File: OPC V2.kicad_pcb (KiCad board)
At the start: 4 copper layers, 65 x 43 mm, 51 parts, among them J1 691382010004, J2 691382010004, J3 691382010004, J4 Conn_01x04_Pin, J6 Conn_01x05, J7 MEC1-110-02-F-D-A, U10 BMP581, U6 ADS1120-PW, U7 MCP23017x-x-ML, U9 DS3231MZ

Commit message: maj puissance
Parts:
- added C13: 0.1µ, Capacitor_SMD:C_0603_1608Metric_Pad1.08x0.95mm_HandSolder, F.Cu at (114.6, 63.6)
- added C14: 0.1µ, Capacitor_SMD:C_0603_1608Metric_Pad1.08x0.95mm_HandSolder, F.Cu at (114.6, 58.5)
- added C15: 4µ7 50V, Capacitor_SMD:C_1206_3216Metric, F.Cu at (150.6, 54.4)
- added C16: 4µ7 50V, Capacitor_SMD:C_1206_3216Metric, F.Cu at (144.2, 54.4)
- added C17: 10µ 10V, Capacitor_SMD:C_0603_1608Metric_Pad1.08x0.95mm_HandSolder, F.Cu at (151.0, 60.1)
- added C18: 1n 2kV, Capacitor_SMD:C_1206_3216Metric, B.Cu at (155.0, 57.2)
- added C19: 0.1µ, Capacitor_SMD:C_0603_1608Metric_Pad1.08x0.95mm_HandSolder, F.Cu at (122.5, 75.4)
- added C20: 0.47µ, Capacitor_SMD:C_0603_1608Metric_Pad1.08x0.95mm_HandSolder, F.Cu at (127.1, 75.4)
- added C21: 10n, Capacitor_SMD:C_0805_2012Metric_Pad1.18x1.45mm_HandSolder, B.Cu at (103.7, 73.9)
- added C22: 10n, Capacitor_SMD:C_0805_2012Metric_Pad1.18x1.45mm_HandSolder, B.Cu at (103.7, 69.3)
- added D3: US1M, Diode_SMD:D_SMA, F.Cu at (114.6, 52.5)
- added D6: US1M, Diode_SMD:D_SMA, B.Cu at (139.1, 88.1)
- added D7: US1M, Diode_SMD:D_SMA, B.Cu at (139.1, 82.3)
- added D8: SMAJ33CA, PCM_Diode_SMD_AKL:D_SMA_TVS, F.Cu at (114.9, 75.4)
- added J5: Screw_Terminal_01x10, TerminalBlock_Phoenix:TerminalBlock_Phoenix_MPT-0,5-10-2.54_1x10_P2.54mm_Horizontal, F.Cu at (106.0, 52.5)
- added J8: MEC1-110-02-F-D-A, OPC:MEC1-110-02-F-D-A-MALE, F.Cu at (173.9, 77.0)
- added J9: Screw_Terminal_01x04, TerminalBlock_Phoenix:TerminalBlock_Phoenix_MPT-0,5-4-2.54_1x04_P2.54mm_Horizontal, F.Cu at (106.0, 82.9)
- added K5: G6DN-1A-L DC24, OPC:G6DN, F.Cu at (132.0, 83.8)
- added K6: G6DN-1A-L DC24, OPC:G6DN, F.Cu at (132.0, 89.6)
- added L1: 1µ 2A, Inductor_SMD:L_1008_2520Metric, F.Cu at (147.4, 55.9)
- added OC2: MOCD217M, PCM_Package_SO_AKL:SO-8_3.9x6.2mm_P1.27mm, F.Cu at (150.0, 86.7)
- added R12: 562, Resistor_SMD:R_0603_1608Metric_Pad0.98x0.95mm_HandSolder, F.Cu at (117.2, 62.7)
- added R13: 2k5, Resistor_SMD:R_0603_1608Metric_Pad0.98x0.95mm_HandSolder, F.Cu at (112.0, 62.7)
- added R14: 2k5, Resistor_SMD:R_0603_1608Metric_Pad0.98x0.95mm_HandSolder, F.Cu at (112.0, 57.6)
- added R15: 562, Resistor_SMD:R_0603_1608Metric_Pad0.98x0.95mm_HandSolder, F.Cu at (117.2, 57.6)
- added R16: 33k, Resistor_SMD:R_0603_1608Metric_Pad0.98x0.95mm_HandSolder, F.Cu at (121.9, 66.8)
- added R23: 1k5, Resistor_SMD:R_0603_1608Metric_Pad0.98x0.95mm_HandSolder, F.Cu at (156.0, 88.6)
- added R24: 1k5, Resistor_SMD:R_0603_1608Metric_Pad0.98x0.95mm_HandSolder, F.Cu at (155.9, 86.1)
- added RV3: MOV-07D391KKTR, Varistor:RV_Disc_D9mm_W3.9mm_P5mm, F.Cu at (118.0, 90.5)
- added RV4: MOV-07D391KKTR, Varistor:RV_Disc_D9mm_W3.9mm_P5mm, F.Cu at (118.0, 85.4)
- added TP1: TestPoint, TestPoint:TestPoint_Pad_2.0x2.0mm, B.Cu at (125.7, 58.8)
- added TP2: TestPoint, TestPoint:TestPoint_Pad_2.0x2.0mm, B.Cu at (125.7, 62.0)
- added U11: SIP-4_1779205311, PCM_MagIC_THT_Wurth:U_Wurth_WPME-FISM-SIP-4_1779405311, F.Cu at (153.0, 53.4)
- added U12: PDRV81545PWPR, OPC:U_TSSOP_PWP0020AC_TEX, F.Cu at (114.9, 69.8)
- added U13: ISO7720D, Package_SO:SOIC-8_3.9x4.9mm_P1.27mm, F.Cu at (133.6, 70.1)
- added U14: TLV75709PDBV, Package_TO_SOT_SMD:SOT-23-5, F.Cu at (124.8, 72.6)
- added U8: ISO1212, Package_SO:SSOP-16_3.9x4.9mm_P0.635mm, F.Cu at (133.6, 60.4)
- C9: footprint Capacitor_SMD:C_0603_1608Metric_Pad1.08x0.95mm_HandSolder -> Capacitor_SMD:C_0603_1608Metric
- R2: value 3k3 -> 16k5
- R3, R4: value 16k5 -> 1M
- renumbered CDiff1 to CDi1, CDiff2 to CDi2
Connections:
- R3 pad 2: GND -> +3V3
- U1 pad 2: AINN -> VREF
- U1 pad 4: VREF -> AINN
- U2 pad 2: AINN -> VREF
- U2 pad 4: VREF -> AINN
- U3 pad 2: AINN -> VREF
- U3 pad 4: VREF -> AINN
- U5 pad 11: VREF -> AINN
- U5 pad 12: 16k5_2 -> TC_GND
- U5 pad 13: 3k3_1 -> 3k3
- U5 pad 5: 3k3_2 -> 16k5
- U5 pad 6: 16k5_1 -> TC_VCC
- U5 pad 8: VREF -> AINP
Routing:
- net AINN: track 79.5 -> 107.1 mm, vias 5 -> 6
- net Net-(J9-Pin_3): track 0.00 -> 26.9 mm
- net Net-(J9-Pin_1): track 0.00 -> 26.8 mm
- net Net-(J9-Pin_2): track 0.00 -> 18.0 mm
- net Net-(J9-Pin_4): track 0.00 -> 18.0 mm
- net AINP: track 84.1 -> 100.9 mm, vias 4 -> 5
- net Net-(D6-A): track 0.00 -> 10.0 mm
- net Net-(D7-A): track 0.00 -> 9.50 mm
- net VREF: track 78.5 -> 86.4 mm, vias 6 -> 5
- net +24V: track 0.00 -> 6.73 mm
- net Net-(OC2-Pad1): track 0.00 -> 2.51 mm
- net Net-(OC2-Pad3): track 0.00 -> 2.41 mm
- net GND1: track 0.00 -> 2.09 mm
- net Net-(U11-+VIN): track 0.00 -> 2.08 mm
- net +3V3: track 65.9 -> 67.6 mm, vias 13 -> 14
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- added copper zone on In1.Cu, net +24V
- added copper zone on In2.Cu, net GND1
- added copper zone on In2.Cu, net GND2
- removed copper zone on B.Cu, net VREF
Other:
- board size 65 x 43 mm -> 65 x 93 mm
- board text added: "+"
- board text added: "-"
- board text added: "1"
- board text added: "2"
- board text added: "In1"
- board text added: "In2"
- board text added: "O1"
- board text added: "O2"
- board text added: "V+"
- board text added: "V-"
- board text added: "Vin"

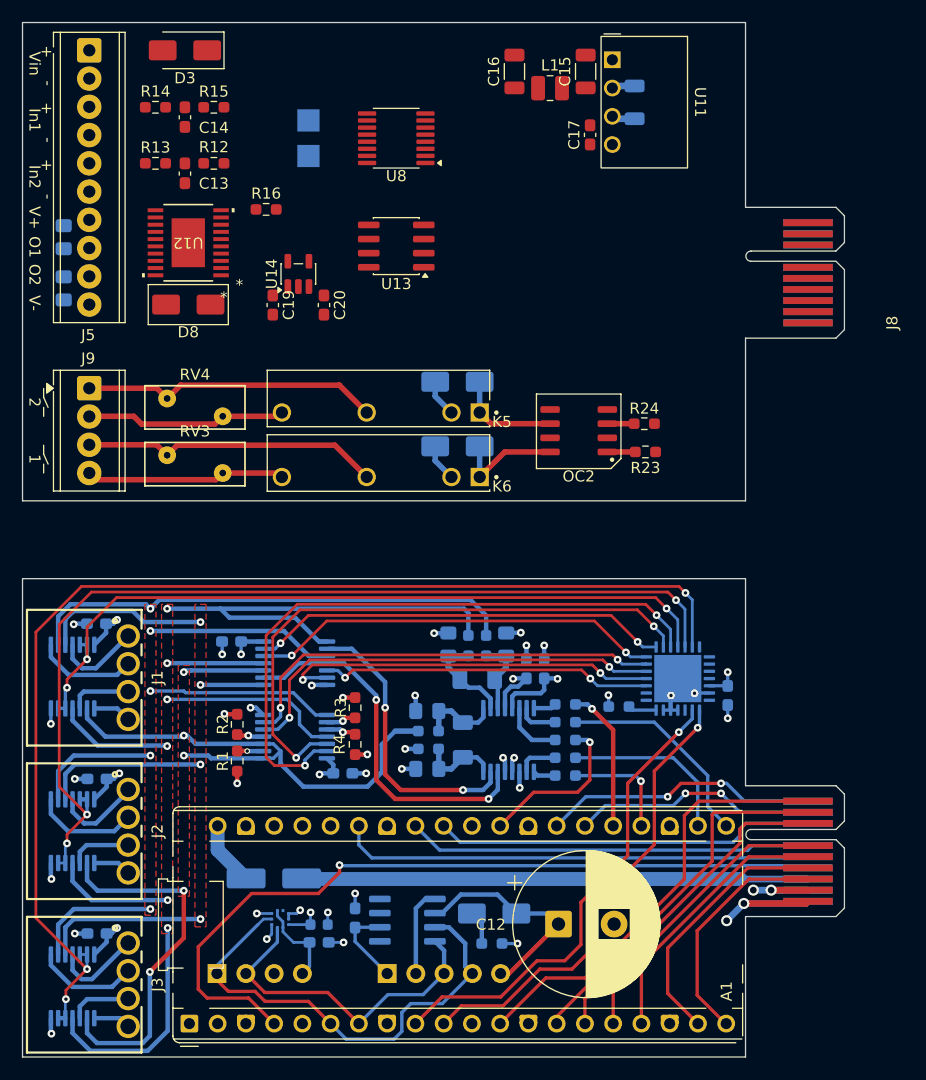
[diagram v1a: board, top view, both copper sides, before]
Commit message: découpage et hierarchie
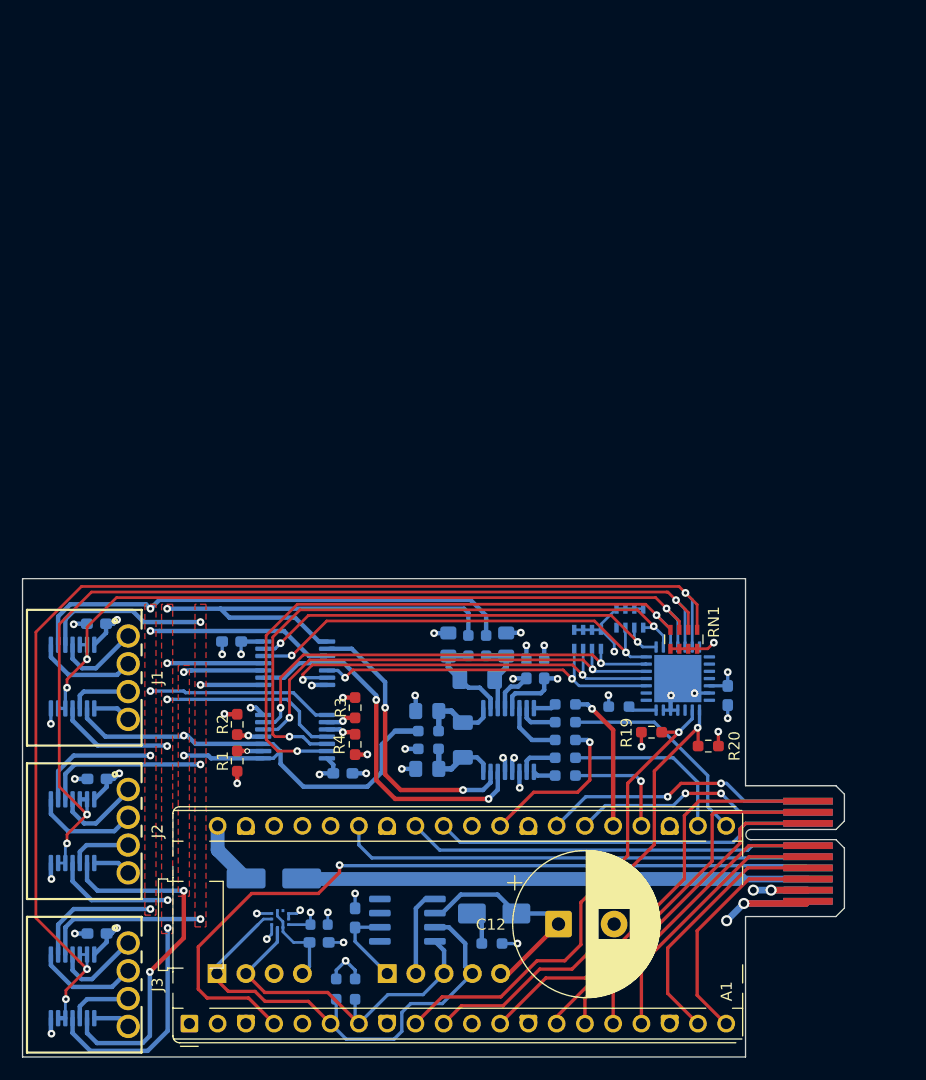
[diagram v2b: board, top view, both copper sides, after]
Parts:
- removed C13, C14, C19: 0.1µ, Capacitor_SMD:C_0603_1608Metric_Pad1.08x0.95mm_HandSolder
- removed C15, C16: 4µ7 50V, Capacitor_SMD:C_1206_3216Metric
- removed C17: 10µ 10V, Capacitor_SMD:C_0603_1608Metric_Pad1.08x0.95mm_HandSolder
- removed C18: 1n 2kV, Capacitor_SMD:C_1206_3216Metric
- removed C20: 0.47µ, Capacitor_SMD:C_0603_1608Metric_Pad1.08x0.95mm_HandSolder
- removed C21, C22: 10n, Capacitor_SMD:C_0805_2012Metric_Pad1.18x1.45mm_HandSolder
- removed D3, D6, D7: US1M, Diode_SMD:D_SMA
- removed D8: SMAJ33CA, PCM_Diode_SMD_AKL:D_SMA_TVS
- removed J5: Screw_Terminal_01x10, TerminalBlock_Phoenix:TerminalBlock_Phoenix_MPT-0,5-10-2.54_1x10_P2.54mm_Horizontal
- removed J8: MEC1-110-02-F-D-A, OPC:MEC1-110-02-F-D-A-MALE
- removed J9: Screw_Terminal_01x04, TerminalBlock_Phoenix:TerminalBlock_Phoenix_MPT-0,5-4-2.54_1x04_P2.54mm_Horizontal
- removed K5, K6: G6DN-1A-L DC24, OPC:G6DN
- removed L1: 1µ 2A, Inductor_SMD:L_1008_2520Metric
- removed OC2: MOCD217M, PCM_Package_SO_AKL:SO-8_3.9x6.2mm_P1.27mm
- removed R12, R15: 562, Resistor_SMD:R_0603_1608Metric_Pad0.98x0.95mm_HandSolder
- removed R13, R14: 2k5, Resistor_SMD:R_0603_1608Metric_Pad0.98x0.95mm_HandSolder
- removed R16: 33k, Resistor_SMD:R_0603_1608Metric_Pad0.98x0.95mm_HandSolder
- removed R23, R24: 1k5, Resistor_SMD:R_0603_1608Metric_Pad0.98x0.95mm_HandSolder
- removed RV3, RV4: MOV-07D391KKTR, Varistor:RV_Disc_D9mm_W3.9mm_P5mm
- removed TP1, TP2: TestPoint, TestPoint:TestPoint_Pad_2.0x2.0mm
- removed U11: SIP-4_1779205311, PCM_MagIC_THT_Wurth:U_Wurth_WPME-FISM-SIP-4_1779405311
- removed U12: PDRV81545PWPR, OPC:U_TSSOP_PWP0020AC_TEX
- removed U13: ISO7720D, Package_SO:SOIC-8_3.9x4.9mm_P1.27mm
- removed U14: TLV75709PDBV, Package_TO_SOT_SMD:SOT-23-5
- removed U8: ISO1212, Package_SO:SSOP-16_3.9x4.9mm_P0.635mm
- added R17: 4k7, Resistor_SMD:R_0603_1608Metric_Pad0.98x0.95mm_HandSolder, B.Cu at (128.2, 136.9)
- added R18: 4k7, Resistor_SMD:R_0603_1608Metric_Pad0.98x0.95mm_HandSolder, B.Cu at (129.9, 136.9)
- added R19: 4k7, Resistor_SMD:R_0603_1608Metric_Pad0.98x0.95mm_HandSolder, F.Cu at (156.6, 113.8)
- added R20: 4k7, Resistor_SMD:R_0603_1608Metric_Pad0.98x0.95mm_HandSolder, F.Cu at (161.7, 115.0)
- added RN1: R_Pack04, Resistor_SMD:R_Array_Concave_4x0603, F.Cu at (159.4, 105.5)
- added RN2: R_Pack04, Resistor_SMD:R_Array_Concave_4x0603, B.Cu at (150.8, 105.5)
- added RN3: R_Pack04, Resistor_SMD:R_Array_Concave_4x0603, B.Cu at (154.6, 103.5)
- R1: value 3.3K -> 1k65
- U1, U2, U3, U4, U5: value ~ -> TS3A4751PWR
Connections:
- net 2_3_WIRE renamed /Entrées/2_3_WIRE
- net 2_WIRE renamed /Entrées/2_WIRE
- net 3_WIRE renamed /Entrées/3_WIRE
- net 4W renamed /Entrées/4W
- net 4_WIRE renamed /Entrées/4_WIRE
- net AIN0 renamed /ADC/AIN0
- net AIN1 renamed /ADC/AIN1
- net AIN2 renamed /ADC/AIN2
- net AIN3 renamed /ADC/AIN3
- net AINN renamed /ADC/AINN
- net AINP renamed /ADC/AINP
- net I2C0_SENSOR_DATA renamed /Pico/I2C0_SENSOR_DATA
- net I2C0_SENSOR_SCK renamed /Pico/I2C0_SENSOR_SCK
- net I2C1_GPIO_DATA renamed /Pico/I2C1_GPIO_DATA
- net I2C1_GPIO_SCK renamed /Pico/I2C1_GPIO_SCK
- net INPUT_1_EN renamed /Entrées/INPUT_1_EN
- net INPUT_2_EN renamed /Entrées/INPUT_2_EN
- net INPUT_3_EN renamed /Entrées/INPUT_3_EN
- net LCD_DC renamed /Connecteur/LCD_DC
- net OUTPUT_1 renamed /Connecteur/OUTPUT_1
- net OUTPUT_2 renamed /Connecteur/OUTPUT_2
- net OUTPUT_3 renamed /Connecteur/OUTPUT_3
- net OUTPUT_4 renamed /Connecteur/OUTPUT_4
- net OUTPUT_5 renamed /Connecteur/OUTPUT_5
- net OUTPUT_6 renamed /Connecteur/OUTPUT_6
- net REFN0 renamed /ADC/REFN0
- net REFP0 renamed /ADC/REFP0
- net ROTENC_A renamed /Connecteur/ROTENC_A
- net ROTENC_B renamed /Connecteur/ROTENC_B
- net ROTENC_CLIC renamed /Connecteur/ROTENC_CLIC
- net SPI0_ADC_MISO renamed /ADC/SPI0_ADC_MISO
- net SPI0_ADC_MOSI renamed /ADC/SPI0_ADC_MOSI
- net SPI0_ADC_SCK renamed /ADC/SPI0_ADC_SCK
- net SPI1_LCD_MOSI renamed /Connecteur/SPI1_LCD_MOSI
- net SPI1_LCD_SCK renamed /Connecteur/SPI1_LCD_SCK
- net VREF renamed /ADC/VREF
- net Vbat renamed /Pico/Vbat
- net /ADC_DRDY renamed /ADC//ADC_DRDY
- net /SPI0_ADC_CS renamed /ADC//SPI0_ADC_CS
- net /SPI1_LCD_CS renamed /Connecteur//SPI1_LCD_CS
- U5 pad 12: TC_GND -> /Entrées/TC_GND
- U5 pad 13: 3k3 -> /Entrées/3k3
- U5 pad 5: 16k5 -> /Entrées/16k5
- U5 pad 6: TC_VCC -> /Entrées/TC_VCC
- U7 pad 19: 3k3_2 -> /Entrées/16k5
- U7 pad 20: 16k5_1 -> /Entrées/TC_VCC
- U7 pad 23: 16k5_2 -> /Entrées/TC_GND
- U7 pad 24: 3k3_1 -> /Entrées/3k3
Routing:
- net 3k3_1: track 57.6 -> 0.00 mm, vias 2 -> 0
- net /Entrées/3k3: track 0.00 -> 57.1 mm, vias 0 -> 2
- net 16k5_2: track 53.1 -> 0.00 mm, vias 2 -> 0
- net /Entrées/TC_GND: track 0.00 -> 53.1 mm, vias 0 -> 2
- net /Entrées/16k5: track 0.00 -> 41.3 mm, vias 0 -> 2
- net /Entrées/TC_VCC: track 0.00 -> 40.7 mm, vias 0 -> 2
- net 3k3_2: track 39.5 -> 0.00 mm, vias 2 -> 0
- net 16k5_1: track 39.4 -> 0.00 mm, vias 2 -> 0
- net Net-(J9-Pin_3): track 26.9 -> 0.00 mm
- net Net-(J9-Pin_1): track 26.8 -> 0.00 mm
- net Net-(J9-Pin_2): track 18.0 -> 0.00 mm
- net Net-(J9-Pin_4): track 18.0 -> 0.00 mm
- net GND: track 63.2 -> 77.0 mm, vias 34 -> 36
- net Net-(D6-A): track 10.0 -> 0.00 mm
- net Net-(D7-A): track 9.50 -> 0.00 mm
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- removed copper zone on In1.Cu, net +24V
- removed copper zone on In2.Cu, net GND1
- removed copper zone on In2.Cu, net GND2
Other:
- board size 65 x 93 mm -> 65 x 43 mm
- board text removed: "+"
- board text removed: "-"
- board text removed: "1"
- board text removed: "2"
- board text removed: "In1"
- board text removed: "In2"
- board text removed: "O1"
- board text removed: "O2"
- board text removed: "V+"
- board text removed: "V-"
- board text removed: "Vin"

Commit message: update
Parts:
- RN1: value R_Pack04 -> 10k; moved to B.Cu
- RN2, RN3: value R_Pack04 -> 10k
- moved RN1 4.01 mm to (163.1, 103.8), turned to 180 degrees
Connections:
- RN1 pad 5: /Entrées/INPUT_3_EN -> /Pico/3k3
- RN1 pad 6: /Entrées/INPUT_2_EN -> /Entrées/INPUT_1_EN
- RN1 pad 7: /Entrées/INPUT_1_EN -> /Entrées/INPUT_2_EN
- RN1 pad 8: /Entrées/3k3 -> /Entrées/INPUT_3_EN
- RN2 pad 6: /Entrées/16k5 -> /Pico/16k5
- U5 pad 13: /Entrées/3k3 -> /Entrées/RREF_1k65
- U5 pad 5: /Entrées/16k5 -> /Entrées/RREF_16k5
- U7 pad 19: /Entrées/16k5 -> /Pico/RREF_16k5
- U7 pad 24: /Entrées/3k3 -> /Pico/RREF_1k65
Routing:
- net /Pico/3k3: track 0.00 -> 61.3 mm, vias 0 -> 3
- net /Entrées/3k3: track 57.1 -> 0.00 mm, vias 2 -> 0
- net /Entrées/16k5: track 41.3 -> 0.00 mm, vias 2 -> 0
- net (no net): track 0.00 -> 41.3 mm, vias 0 -> 2
- net /Entrées/INPUT_1_EN: track 70.6 -> 73.2 mm, vias 3 -> 4
- net /Entrées/INPUT_2_EN: track 90.6 -> 91.6 mm, vias 3 -> 4
- net /Entrées/INPUT_3_EN: track 109.2 -> 108.7 mm

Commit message: suite et nouvel écran
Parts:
- removed R19, R20: 4k7, Resistor_SMD:R_0603_1608Metric_Pad0.98x0.95mm_HandSolder
- added R6: 3k3, Resistor_SMD:R_0603_1608Metric_Pad0.98x0.95mm_HandSolder, F.Cu at (117.8, 116.4)
- D1: footprint Diode_SMD:D_SMA_Handsoldering -> Diode_SMD:D_SMA
- R7: renamed from R1; value 1k65 -> 3k3
- renumbered C12 to C1, C9 to C10, C3 to C11, C8 to C12, C1 to C2, C4 to C3, C6 to C4, C7 to C5, C11 to C6, C5 to C7, C2 to C8, C10 to C9, J7 to J3, J3 to J4, J6 to J5, J4 to J6, R3 to R1, R7 to R10, R9 to R11, R8 to R12, R5 to R13, R11 to R14, R18 to R15, R17 to R16, R6 to R8, R10 to R9, RN3 to RN1, RN1 to RN2, RN2 to RN3, U4 to U1, U1 to U2, U7 to U3, U5 to U4, U6 to U5, U2 to U6, U10 to U7, U9 to U8, U3 to U9
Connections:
- A1 pad 10: /Pico/I2C1_GPIO_SCK -> /Pico/I2C1_SCK
- A1 pad 11: unconnected-(A1-GPIO8-Pad11) -> /Connecteur/OUTPUT_5
- A1 pad 12: /Connecteur/ROTENC_CLIC -> /Connecteur/OUTPUT_6
- A1 pad 32: /Connecteur/OUTPUT_5 -> /Connecteur/OUTPUT_4
- A1 pad 34: /Connecteur/OUTPUT_6 -> /Connecteur/ROTENC_CLIC
- A1 pad 4: /Connecteur/OUTPUT_4 -> unconnected-(A1-GPIO2-Pad4)
- A1 pad 6: /Pico/I2C0_SENSOR_DATA -> unconnected-(A1-GPIO4-Pad6)
- A1 pad 7: /Pico/I2C0_SENSOR_SCK -> unconnected-(A1-GPIO5-Pad7)
- A1 pad 9: /Pico/I2C1_GPIO_DATA -> /Pico/I2C1_DATA
- J3 pad 08: /Connecteur/OUTPUT_4 -> /Connecteur/OUTPUT_6
- J3 pad 10: /Connecteur/OUTPUT_6 -> /Connecteur/OUTPUT_5
- J3 pad 12: /Connecteur/OUTPUT_5 -> /Connecteur/OUTPUT_4
- J5 pad 3: /Pico/I2C0_SENSOR_SCK -> /Pico/I2C1_SCK
- J5 pad 4: /Pico/I2C0_SENSOR_DATA -> /Pico/I2C1_DATA
- J6 pad 1: /Pico/I2C0_SENSOR_DATA -> /Pico/I2C1_DATA
- J6 pad 2: /Pico/I2C0_SENSOR_SCK -> /Pico/I2C1_SCK
- R15 pad 1: /Pico/I2C0_SENSOR_SCK -> /Pico/I2C1_SCK
- R16 pad 1: /Pico/I2C0_SENSOR_DATA -> /Pico/I2C1_DATA
- U3 pad 8: /Pico/I2C1_GPIO_SCK -> /Pico/I2C1_SCK
- U3 pad 9: /Pico/I2C1_GPIO_DATA -> /Pico/I2C1_DATA
- U7 pad 2: /Pico/I2C0_SENSOR_SCK -> /Pico/I2C1_SCK
- U7 pad 4: /Pico/I2C0_SENSOR_DATA -> /Pico/I2C1_DATA
- U8 pad 7: /Pico/I2C0_SENSOR_DATA -> /Pico/I2C1_DATA
- U8 pad 8: /Pico/I2C0_SENSOR_SCK -> /Pico/I2C1_SCK
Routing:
- net /Pico/I2C1_DATA: track 0.00 -> 87.3 mm, vias 0 -> 1
- net /Pico/I2C1_SCK: track 0.00 -> 83.6 mm, vias 0 -> 1
- net /Pico/I2C1_GPIO_DATA: track 45.3 -> 0.00 mm, vias 1 -> 0
- net /Pico/I2C0_SENSOR_DATA: track 45.2 -> 0.00 mm
- net /Pico/I2C1_GPIO_SCK: track 43.3 -> 0.00 mm, vias 1 -> 0
- net /Connecteur/OUTPUT_4: track 70.2 -> 36.4 mm, vias 1 -> 0
- net /Pico/I2C0_SENSOR_SCK: track 32.4 -> 0.00 mm
- net +3V3: track 74.1 -> 57.6 mm, vias 17 -> 18
- net GND: track 76.5 -> 70.1 mm, vias 36 -> 39
- net /Connecteur/OUTPUT_6: track 42.6 -> 36.4 mm, vias 0 -> 1
- net /Connecteur/ROTENC_CLIC: track 39.3 -> 43.4 mm, vias 0 -> 1
- net /Connecteur/OUTPUT_5: track 36.4 -> 39.4 mm, vias 0 -> 1
- net /Connecteur/SPI1_LCD_SCK: track 23.5 -> 21.5 mm
- net +5V: track 44.1 -> 46.0 mm
- net Net-(U4-COM1): track 2.34 -> 3.89 mm
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- added copper zone on B.Cu, net +3V3
- added copper zone on F.Cu, net +3V3
- added copper zone on B.Cu, net GND
- added copper zone on F.Cu, net GND
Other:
- board text added: "JLCJLCJLC"
- board text added: "OPC V0.2 - GaOu 2026"

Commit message: corrections
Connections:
- RN2 pad 5: /Pico/3k3 -> /Entrées/RREF_16k5
- RN3 pad 6: /Pico/16k5 -> /Entrées/RREF_1k65
- U3 pad 19: /Pico/RREF_16k5 -> /Entrées/RREF_1k65
- U3 pad 24: /Pico/RREF_1k65 -> /Entrées/RREF_16k5
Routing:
- net /Pico/3k3: track 61.3 -> 0.00 mm, vias 3 -> 0
- net /Entrées/RREF_16k5: track 0.00 -> 56.3 mm, vias 0 -> 3
- net /Entrées/RREF_1k65: track 0.00 -> 43.7 mm, vias 0 -> 2
- net (no net): track 41.3 -> 0.00 mm, vias 2 -> 0
- net /Entrées/TC_GND: track 53.1 -> 51.9 mm
- net /ADC/VREF: track 86.4 -> 85.7 mm

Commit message: daily
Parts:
- R10: renamed from R6; moved to B.Cu
- R3: renamed from R1; moved to B.Cu
- R5: renamed from R2; moved to B.Cu
- R7: renamed from R4; moved to B.Cu
- R9: renamed from R7; moved to B.Cu
- moved R5 0.66 mm to (118.7, 113.0)
- moved R9 0.21 mm to (119.5, 116.5)
- moved R10 0.07 mm to (117.8, 116.5)
- renumbered R8 to R1, R13 to R11, R14 to R12, R15 to R13, R16 to R14, R9 to R2, R10 to R4, R11 to R6, R12 to R8
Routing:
- net /ADC/AINN: track 107.1 -> 100.0 mm
- net /ADC/VREF: track 85.7 -> 83.4 mm
- net /Entrées/4_WIRE: track 36.9 -> 35.2 mm
- net GND: track 69.9 -> 68.6 mm, vias 39 -> 40
- net /ADC/AIN3: track 33.1 -> 33.9 mm
- net +3V3: track 57.6 -> 56.9 mm
- net Net-(U4-COM2): track 2.43 -> 3.11 mm, vias 1 -> 0
- net Net-(U4-COM1): track 3.89 -> 3.85 mm, vias 1 -> 0
- net Net-(U4-COM4): vias 1 -> 0
- net Net-(U4-COM3): vias 1 -> 0

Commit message: avant prod
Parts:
- C10, C11, C12, C2, C3, C4, C5, C6, C7, C8, C9: value 0.1µ -> 0.1µ 10V
- R10, R3, R5, R7, R9: footprint Resistor_SMD:R_0603_1608Metric_Pad0.98x0.95mm_HandSolder -> Resistor_SMD:R_0805_2012Metric
- moved R10 0.10 mm to (117.7, 116.5)
- moved R9 0.10 mm to (119.6, 116.5)
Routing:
- net /Entrées/RREF_16k5: track 56.3 -> 54.6 mm
- net /Entrées/2_WIRE: track 39.3 -> 40.6 mm
- net /Entrées/INPUT_1_EN: track 73.2 -> 74.4 mm
- net /Entrées/TC_VCC: track 40.7 -> 41.7 mm
- net /Entrées/INPUT_3_EN: track 108.7 -> 109.5 mm
- net /Entrées/4_WIRE: track 35.2 -> 35.9 mm
- net GND: track 68.6 -> 68.0 mm
